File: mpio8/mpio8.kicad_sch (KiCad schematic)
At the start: 80 parts, among them J1 Conn_01x02_Male, J10 Conn_01x04_Male, J11 Conn_01x04_Male, J2 JST PHR4 (STEMMA), J3 Conn_02x05_Odd_Even, J4 Conn_01x02_Male, J5 Conn_01x02_Male, J6 Conn_01x02_Male, J7 Conn_01x02_Male, J8 Conn_01x04_Male, J9 Conn_01x04_Male, K1 J102-1C, K2 J102-1C, K3 J102-1C, K4 J102-1C, Q1 IRLZ44N, Q10 MMBT3904, Q2 MMBT3904, Q3 IRLZ44N, Q4 MMBT3904, Q5 IRLZ44N, Q6 MMBT3904, Q7 IRLZ44N, Q8 MMBT3904, Q9 MMBT3904, U1 TCA9554DW, U2 MIC4427, U3 MIC4427, U4 PC817, U5 PC817, U6 PC817, U7 PC817

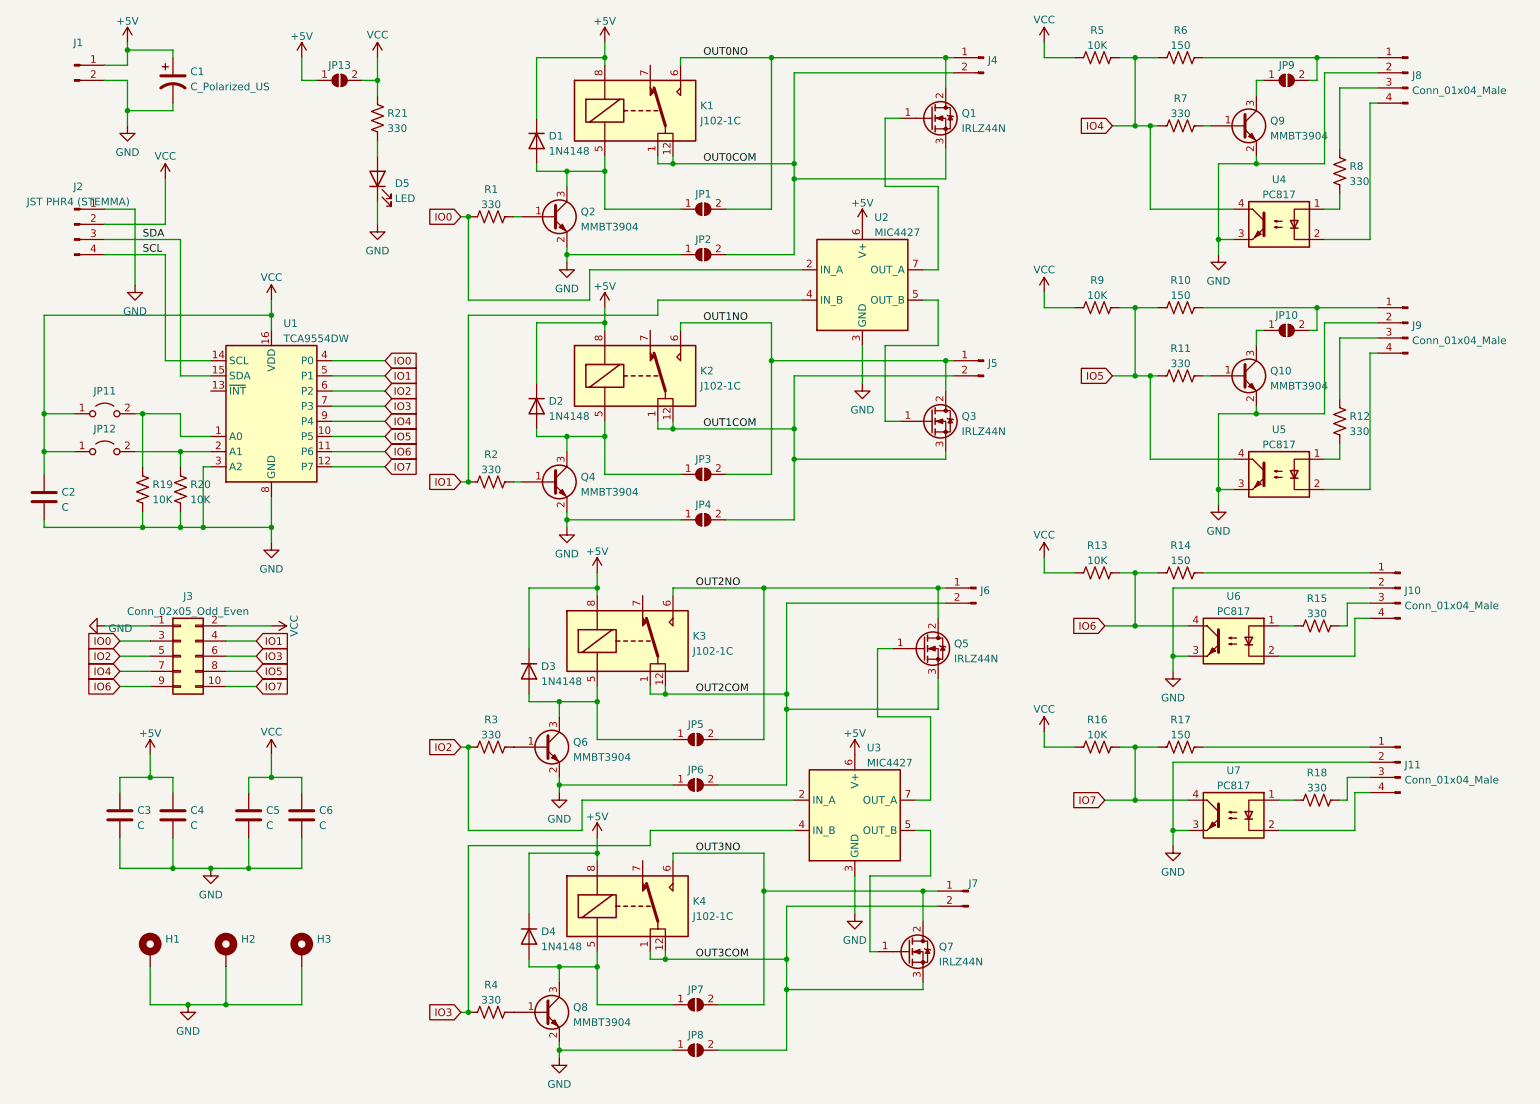
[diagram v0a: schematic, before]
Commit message: mpio8: r1.1
 - fix I2C connector pinout
 - DIP switch for address pins
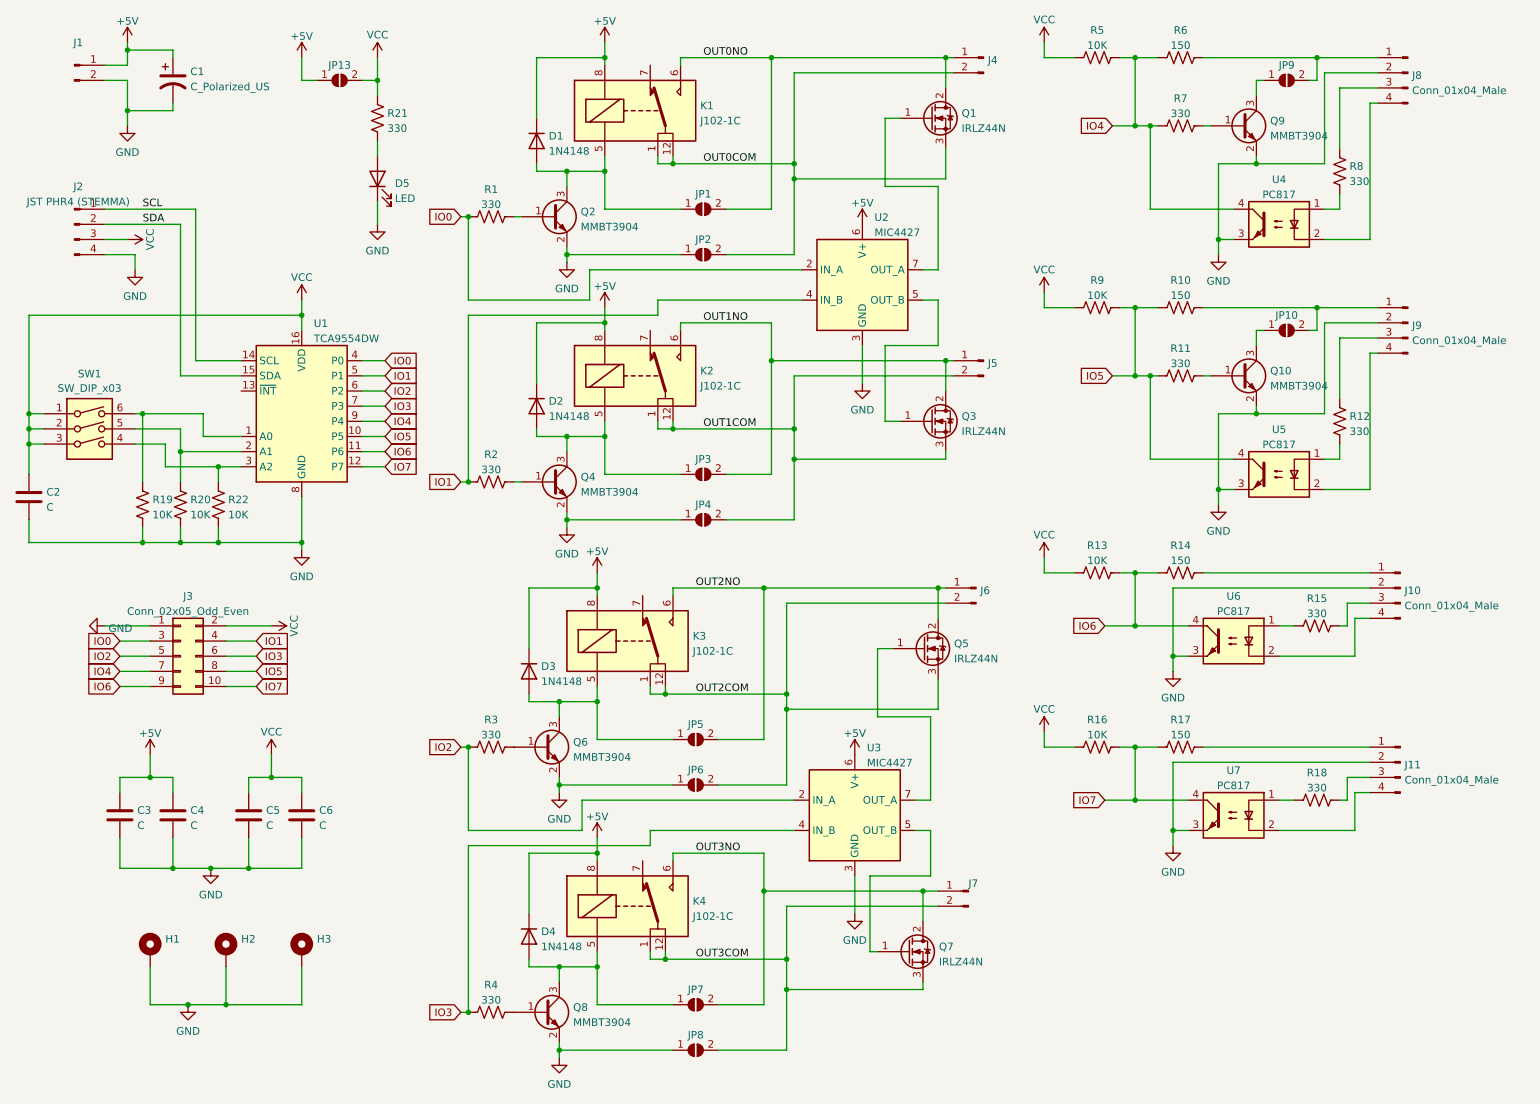
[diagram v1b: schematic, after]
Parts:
- removed JP11, JP12: Jumper_2_Open, Connector_PinHeader_2.00mm:PinHeader_1x02_P2.00mm_Vertical, symbol Jumper:Jumper_2_Open
- added R22: 10K, Resistor_SMD:R_0805_2012Metric, symbol Device:R_US
- added SW1: SW_DIP_x03, Button_Switch_THT:SW_DIP_SPSTx03_Slide_6.7x9.18mm_W7.62mm_P2.54mm_LowProfile, symbol Switch:SW_DIP_x03
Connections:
- net GND: now also J2.4 (Pin_4), R22.1; no longer J2.1 (Pin_1), U1.3 (A2)
- net SCL: now also J2.1 (Pin_1); no longer J2.4 (Pin_4)
- net SDA: now also J2.2 (Pin_2); no longer J2.3 (Pin_3)
- net VCC: now also J2.3 (Pin_3), SW1.1, SW1.2, SW1.3; no longer J2.2 (Pin_2)
- net at R20.2, U1.2 (A1): now also SW1.5
- net at R19.2, U1.1 (A0): now also SW1.6
- new net: R22.2, SW1.4, U1.3 (A2)
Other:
- title: (none) -> Multi-Personality IO Board
- moved on the sheet: C2, R19, R20, U1
